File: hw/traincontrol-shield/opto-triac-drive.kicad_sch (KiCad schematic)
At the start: 6 parts, among them U5 MOC3021M, U6 MOC3021M

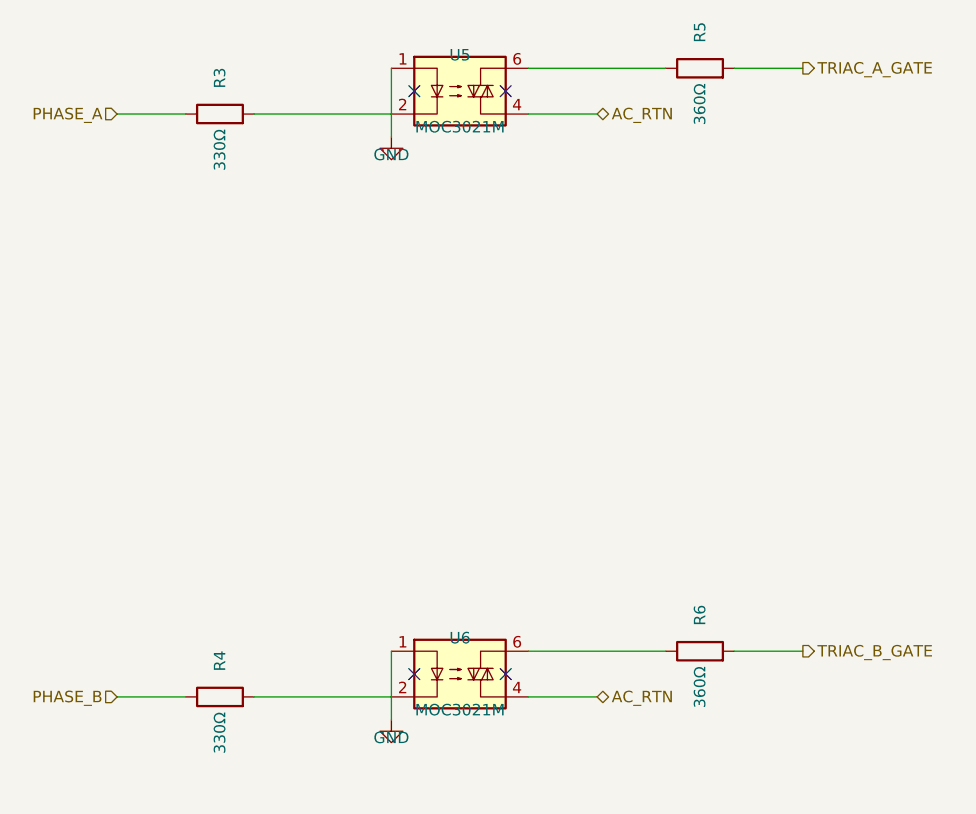
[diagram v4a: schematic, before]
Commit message: Fix schematic ERC errors: pin Y-flip, PWR_FLAG, label wiring, spacing
- Fix connector pin positions using Y-flip convention (sym Y-up → sch Y-down)
- Add GND PWR_FLAG to power-supply sheet (eliminates power_pin_not_driven)
- Fix top-level connector label placement: labels at stub end, wires toward pins
- Apply omnidirectional spacing and IC-to-passive body gap rules across sheets
- Update schematics-plan.md with ERC workflow and coordinate conventions
- Regenerate all sub-sheets with corrected generator scripts

ERC result: 138 violations (all warnings/cosmetic), 0 critical errors.

Co-Authored-By: Claude Opus 4.6 <noreply@anthropic.com>
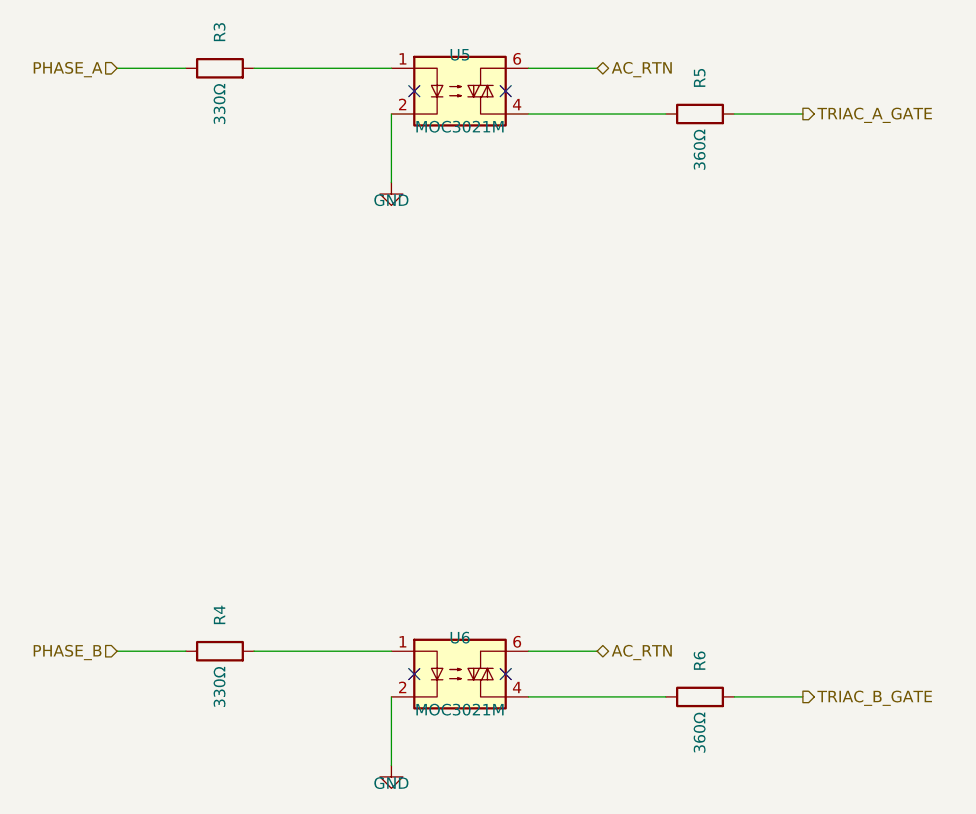
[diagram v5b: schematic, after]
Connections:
- net AC_RTN: now also U5.6, U6.6; no longer U5.4, U6.4
- net GND: now also U5.2, U6.2; no longer U5.1, U6.1
- net at R3.2: now also U5.1; no longer U5.2
- net at R5.1: now also U5.4; no longer U5.6
- net at R4.2: now also U6.1; no longer U6.2
- net at R6.1: now also U6.4; no longer U6.6
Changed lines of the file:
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@@
 	)
 	(wire
-		(pts (xy 72.39 87.63) (xy 72.39 95.25))
+		(pts (xy 72.39 92.71000000000001) (xy 72.39 100.33000000000001))
 		(stroke (width 0) (type solid))
 	)
 	(symbol
 		(lib_id "power:GND")
-		(at 72.39 95.25 0)
+		(at 72.39 100.33000000000001 0)
 		(unit 1)
 		(exclude_from_sim no)
@@
 		(dnp no)
 		(property "Reference" "#PWR0503"
-			(at 72.39 93.25 0)
+			(at 72.39 98.33000000000001 0)
 			(effects (font (size 1.27 1.27)) (hide yes))
 		)
 		(property "Value" "GND"
-			(at 72.39 97.25 0)
+			(at 72.39 102.33000000000001 0)
 			(effects (font (size 1.27 1.27)))
 		)
 		(property "Footprint" ""
-			(at 72.39 95.25 0)
+			(at 72.39 100.33000000000001 0)
 			(effects (font (size 1.27 1.27)) (hide yes))
 		)
 		(property "Datasheet" ""
-			(at 72.39 95.25 0)
+			(at 72.39 100.33000000000001 0)
 			(effects (font (size 1.27 1.27)) (hide yes))
 		)
@@
 	)
 	(wire
-		(pts (xy 87.63000000000001 92.71000000000001) (xy 95.25000000000001 92.71000000000001))
+		(pts (xy 87.63000000000001 87.63) (xy 95.25000000000001 87.63))
 		(stroke (width 0) (type solid))
 	)
 	(hierarchical_label "AC_RTN"
 		(shape bidirectional)
-		(at 95.25000000000001 92.71000000000001 0)
+		(at 95.25000000000001 87.63 0)
 		(fields_autoplaced yes)
 		(effects (font (size 1.27 1.27)) (justify left bottom))
 		(property "Intersheetrefs" "${INTERSHEET_REFS}"
-			(at 95.25000000000001 92.71000000000001 0)
+			(at 95.25000000000001 87.63 0)
 			(effects (font (size 1.27 1.27)) (hide yes))
 		)
@@
 	(symbol
 		(lib_id "Device:R")
-		(at 53.339999999999996 92.71000000000001 90)
+		(at 53.339999999999996 87.63 90)
 		(unit 1)
 		(exclude_from_sim no)
@@
 		(dnp no)
 		(property "Reference" "R3"
-			(at 53.339999999999996 88.71000000000001 0)
+			(at 53.339999999999996 83.63 0)
 			(effects (font (size 1.27 1.27)))
 		)
 		(property "Value" "330Ω"
-			(at 53.339999999999996 96.71000000000001 0)
+			(at 53.339999999999996 91.63 0)
 			(effects (font (size 1.27 1.27)))
 		)
 		(property "Footprint" "Resistor_SMD:R_0603_1608Metric"
-			(at 53.339999999999996 92.71000000000001 0)
-			(effects (font (size 1.27 1.27)) (hide yes))
-		)
-		(property "Datasheet" "~"
-			(at 53.339999999999996 92.71000000000001 0)
+			(at 53.339999999999996 87.63 0)
+			(effects (font (size 1.27 1.27)) (hide yes))
+		)
+		(property "Datasheet" "~"
+			(at 53.339999999999996 87.63 0)
 			(effects (font (size 1.27 1.27)) (hide yes))
 		)
@@
 	)
 	(wire
-		(pts (xy 57.15 92.71000000000001) (xy 72.39 92.71000000000001))
-		(stroke (width 0) (type solid))
-	)
-	(wire
-		(pts (xy 41.91 92.71000000000001) (xy 49.529999999999994 92.71000000000001))
+		(pts (xy 57.15 87.63) (xy 72.39 87.63))
+		(stroke (width 0) (type solid))
+	)
+	(wire
+		(pts (xy 41.91 87.63) (xy 49.529999999999994 87.63))
 		(stroke (width 0) (type solid))
 	)
 	(hierarchical_label "PHASE_A"
 		(shape input)
-		(at 41.91 92.71000000000001 180)
+		(at 41.91 87.63 180)
 		(fields_autoplaced yes)
 		(effects (font (size 1.27 1.27)) (justify right bottom))
 		(property "Intersheetrefs" "${INTERSHEET_REFS}"
-			(at 41.91 92.71000000000001 0)
+			(at 41.91 87.63 0)
 			(effects (font (size 1.27 1.27)) (hide yes))
 		)
@@
 	(symbol
 		(lib_id "Device:R")
-		(at 106.68 87.63 90)
+		(at 106.68 92.71000000000001 90)
 		(unit 1)
 		(exclude_from_sim no)
@@
 		(dnp no)
 		(property "Reference" "R5"
-			(at 106.68 83.63 0)
+			(at 106.68 88.71000000000001 0)
 			(effects (font (size 1.27 1.27)))
 		)
 		(property "Value" "360Ω"
-			(at 106.68 91.63 0)
+			(at 106.68 96.71000000000001 0)
 			(effects (font (size 1.27 1.27)))
 		)
 		(property "Footprint" "Resistor_SMD:R_0603_1608Metric"
-			(at 106.68 87.63 0)
-			(effects (font (size 1.27 1.27)) (hide yes))
-		)
-		(property "Datasheet" "~"
-			(at 106.68 87.63 0)
+			(at 106.68 92.71000000000001 0)
+			(effects (font (size 1.27 1.27)) (hide yes))
+		)
+		(property "Datasheet" "~"
+			(at 106.68 92.71000000000001 0)
 			(effects (font (size 1.27 1.27)) (hide yes))
 		)
@@
 	)
 	(wire
-		(pts (xy 87.63000000000001 87.63) (xy 102.87 87.63))
-		(stroke (width 0) (type solid))
-	)
-	(wire
-		(pts (xy 110.49000000000001 87.63) (xy 118.11000000000001 87.63))
+		(pts (xy 87.63000000000001 92.71000000000001) (xy 102.87 92.71000000000001))
+		(stroke (width 0) (type solid))
+	)
+	(wire
+		(pts (xy 110.49000000000001 92.71000000000001) (xy 118.11000000000001 92.71000000000001))
 		(stroke (width 0) (type solid))
 	)
 	(hierarchical_label "TRIAC_A_GATE"
 		(shape output)
-		(at 118.11000000000001 87.63 0)
+		(at 118.11000000000001 92.71000000000001 0)
 		(fields_autoplaced yes)
 		(effects (font (size 1.27 1.27)) (justify left bottom))
 		(property "Intersheetrefs" "${INTERSHEET_REFS}"
-			(at 118.11000000000001 87.63 0)
+			(at 118.11000000000001 92.71000000000001 0)
 			(effects (font (size 1.27 1.27)) (hide yes))
 		)
@@
 	)
 	(wire
-		(pts (xy 72.39 152.4) (xy 72.39 160.02))
+		(pts (xy 72.39 157.48) (xy 72.39 165.1))
 		(stroke (width 0) (type solid))
 	)
 	(symbol
 		(lib_id "power:GND")
-		(at 72.39 160.02 0)
+		(at 72.39 165.1 0)
 		(unit 1)
 		(exclude_from_sim no)
@@
 		(dnp no)
 		(property "Reference" "#PWR0504"
-			(at 72.39 158.02 0)
+			(at 72.39 163.1 0)
 			(effects (font (size 1.27 1.27)) (hide yes))
 		)
 		(property "Value" "GND"
-			(at 72.39 162.02 0)
+			(at 72.39 167.1 0)
 			(effects (font (size 1.27 1.27)))
 		)
 		(property "Footprint" ""
-			(at 72.39 160.02 0)
+			(at 72.39 165.1 0)
 			(effects (font (size 1.27 1.27)) (hide yes))
 		)
 		(property "Datasheet" ""
-			(at 72.39 160.02 0)
+			(at 72.39 165.1 0)
 			(effects (font (size 1.27 1.27)) (hide yes))
 		)
@@
 	)
 	(wire
-		(pts (xy 87.63000000000001 157.48) (xy 95.25000000000001 157.48))
+		(pts (xy 87.63000000000001 152.4) (xy 95.25000000000001 152.4))
 		(stroke (width 0) (type solid))
 	)
 	(hierarchical_label "AC_RTN"
 		(shape bidirectional)
-		(at 95.25000000000001 157.48 0)
+		(at 95.25000000000001 152.4 0)
 		(fields_autoplaced yes)
 		(effects (font (size 1.27 1.27)) (justify left bottom))
 		(property "Intersheetrefs" "${INTERSHEET_REFS}"
-			(at 95.25000000000001 157.48 0)
+			(at 95.25000000000001 152.4 0)
 			(effects (font (size 1.27 1.27)) (hide yes))
 		)
@@
 	(symbol
 		(lib_id "Device:R")
-		(at 53.339999999999996 157.48 90)
+		(at 53.339999999999996 152.4 90)
 		(unit 1)
 		(exclude_from_sim no)
@@
 		(dnp no)
 		(property "Reference" "R4"
-			(at 53.339999999999996 153.48 0)
+			(at 53.339999999999996 148.4 0)
 			(effects (font (size 1.27 1.27)))
 		)
 		(property "Value" "330Ω"
-			(at 53.339999999999996 161.48 0)
+			(at 53.339999999999996 156.4 0)
 			(effects (font (size 1.27 1.27)))
 		)
 		(property "Footprint" "Resistor_SMD:R_0603_1608Metric"
-			(at 53.339999999999996 157.48 0)
-			(effects (font (size 1.27 1.27)) (hide yes))
-		)
-		(property "Datasheet" "~"
-			(at 53.339999999999996 157.48 0)
+			(at 53.339999999999996 152.4 0)
+			(effects (font (size 1.27 1.27)) (hide yes))
+		)
+		(property "Datasheet" "~"
+			(at 53.339999999999996 152.4 0)
 			(effects (font (size 1.27 1.27)) (hide yes))
 		)
@@
 	)
 	(wire
-		(pts (xy 57.15 157.48) (xy 72.39 157.48))
-		(stroke (width 0) (type solid))
-	)
-	(wire
-		(pts (xy 41.91 157.48) (xy 49.529999999999994 157.48))
+		(pts (xy 57.15 152.4) (xy 72.39 152.4))
+		(stroke (width 0) (type solid))
+	)
+	(wire
+		(pts (xy 41.91 152.4) (xy 49.529999999999994 152.4))
 		(stroke (width 0) (type solid))
 	)
 	(hierarchical_label "PHASE_B"
 		(shape input)
-		(at 41.91 157.48 180)
+		(at 41.91 152.4 180)
 		(fields_autoplaced yes)
 		(effects (font (size 1.27 1.27)) (justify right bottom))
 		(property "Intersheetrefs" "${INTERSHEET_REFS}"
-			(at 41.91 157.48 0)
+			(at 41.91 152.4 0)
 			(effects (font (size 1.27 1.27)) (hide yes))
 		)
@@
 	(symbol
 		(lib_id "Device:R")
-		(at 106.68 152.4 90)
+		(at 106.68 157.48 90)
 		(unit 1)
 		(exclude_from_sim no)
@@
 		(dnp no)
 		(property "Reference" "R6"
-			(at 106.68 148.4 0)
+			(at 106.68 153.48 0)
 			(effects (font (size 1.27 1.27)))
 		)
 		(property "Value" "360Ω"
-			(at 106.68 156.4 0)
+			(at 106.68 161.48 0)
 			(effects (font (size 1.27 1.27)))
 		)
 		(property "Footprint" "Resistor_SMD:R_0603_1608Metric"
-			(at 106.68 152.4 0)
-			(effects (font (size 1.27 1.27)) (hide yes))
-		)
-		(property "Datasheet" "~"
-			(at 106.68 152.4 0)
+			(at 106.68 157.48 0)
+			(effects (font (size 1.27 1.27)) (hide yes))
+		)
+		(property "Datasheet" "~"
+			(at 106.68 157.48 0)
 			(effects (font (size 1.27 1.27)) (hide yes))
 		)
@@
 	)
 	(wire
-		(pts (xy 87.63000000000001 152.4) (xy 102.87 152.4))
-		(stroke (width 0) (type solid))
-	)
-	(wire
-		(pts (xy 110.49000000000001 152.4) (xy 118.11000000000001 152.4))
+		(pts (xy 87.63000000000001 157.48) (xy 102.87 157.48))
+		(stroke (width 0) (type solid))
+	)
+	(wire
+		(pts (xy 110.49000000000001 157.48) (xy 118.11000000000001 157.48))
 		(stroke (width 0) (type solid))
 	)
 	(hierarchical_label "TRIAC_B_GATE"
 		(shape output)
-		(at 118.11000000000001 152.4 0)
+		(at 118.11000000000001 157.48 0)
 		(fields_autoplaced yes)
 		(effects (font (size 1.27 1.27)) (justify left bottom))
 		(property "Intersheetrefs" "${INTERSHEET_REFS}"
-			(at 118.11000000000001 152.4 0)
-			(effects (font (size 1.27 1.27)) (hide yes))
-		)
+			(at 118.11000000000001 157.48 0)
+			(effects (font (size 1.27 1.27)) (hide yes))
+		)
